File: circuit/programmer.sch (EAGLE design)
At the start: 23 parts, among them U1 TEENSY_3.0_DIL, X1 ESP01, X2 DIRTCHEAPRX-PROG-MINI, X3 DIRTCHEAPRX-PROG-NANO, X4 ESP01

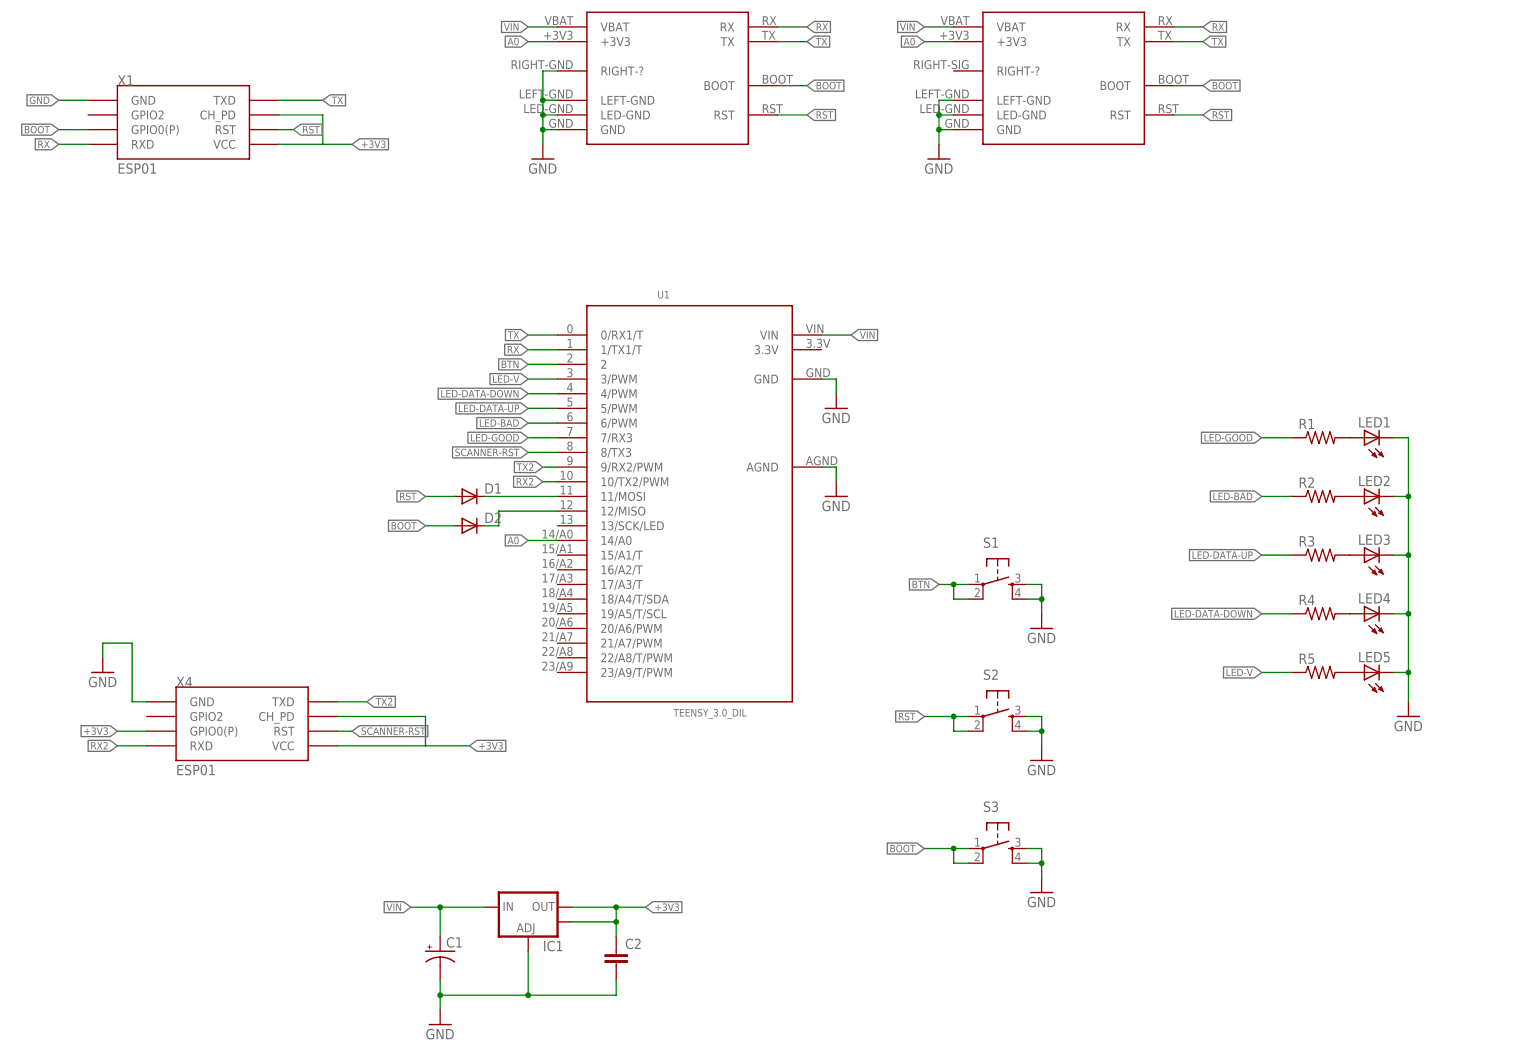
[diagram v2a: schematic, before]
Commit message: programmer, more vias, disconnectable boot signal
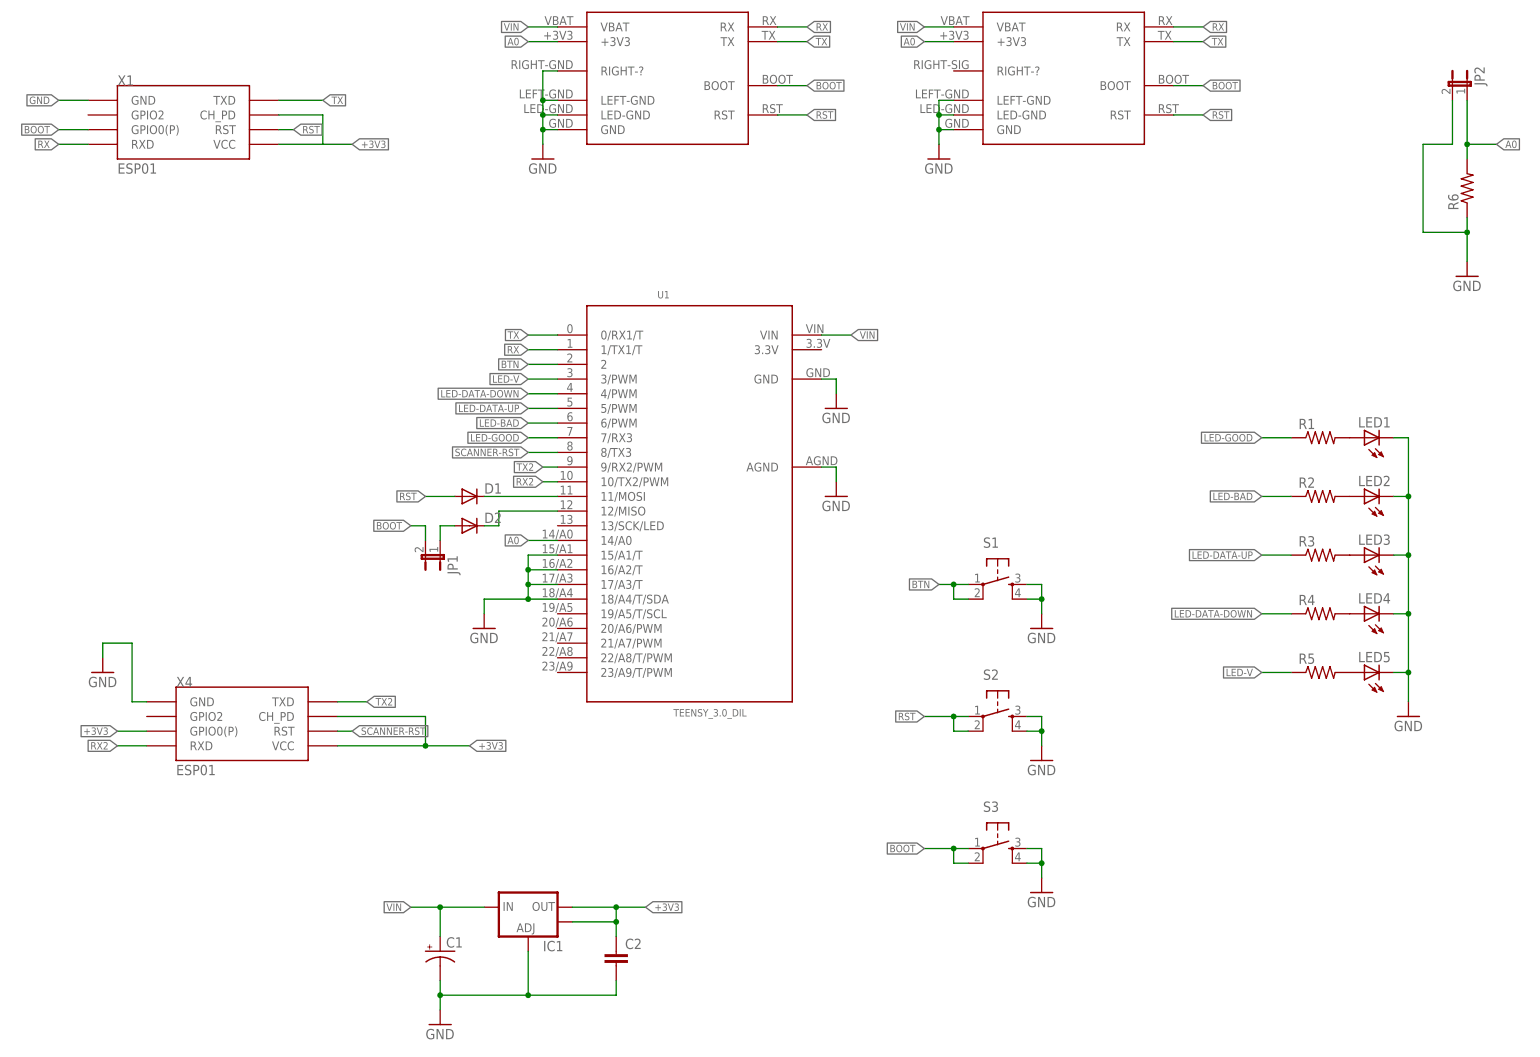
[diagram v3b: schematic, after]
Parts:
- added JP1, JP2: (no value), dirtcheaprx:JUMPER-2PTH_LOCK
- added R6: (no value), dirtcheaprx:RESISTOR0603-RES
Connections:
- new net N$8: D2.A, JP1.1
- net A0: now also JP2.1, R6.2
- net BOOT: now also JP1.2; no longer D2.A
- net GND: now also JP2.2, R6.1, U1.15/A1/T, U1.16/A2/T, U1.17/A3/T, U1.18/A4/T/SDA
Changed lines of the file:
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@@
 <part name="C1" library="dirtcheaprx" deviceset="CAP_POL" device="PTH1"/>
 <part name="C2" library="dirtcheaprx" deviceset="CAP" device="PTH2"/>
+<part name="JP1" library="dirtcheaprx" deviceset="JUMPER-2" device="PTH_LOCK"/>
+<part name="GND11" library="dirtcheaprx" deviceset="GND" device=""/>
+<part name="R6" library="dirtcheaprx" deviceset="RESISTOR" device="0603-RES"/>
+<part name="GND12" library="dirtcheaprx" deviceset="GND" device=""/>
+<part name="JP2" library="dirtcheaprx" deviceset="JUMPER-2" device="PTH_LOCK"/>
 </parts>
 <sheets>
@@
 <instance part="C1" gate="G$1" x="86.36" y="-66.04"/>
 <instance part="C2" gate="G$1" x="116.84" y="-68.58"/>
+<instance part="JP1" gate="A" x="86.36" y="2.54" rot="R180"/>
+<instance part="GND11" gate="1" x="93.98" y="-10.16"/>
+<instance part="R6" gate="G$1" x="264.16" y="66.04" rot="R90"/>
+<instance part="GND12" gate="1" x="264.16" y="50.8"/>
+<instance part="JP2" gate="A" x="264.16" y="83.82" rot="MR0"/>
 </instances>
 <busses>
@@
 <wire x1="83.82" y1="-25.4" x2="83.82" y2="-30.48" width="0.1524" layer="91"/>
 <label x="91.44" y="-30.48" size="1.27" layer="95" xref="yes"/>
+<junction x="83.82" y="-30.48"/>
 </segment>
 <segment>
@@
 </segment>
 <segment>
-<pinref part="D2" gate="G$1" pin="A"/>
-<wire x1="88.9" y1="7.62" x2="83.82" y2="7.62" width="0.1524" layer="91"/>
-<label x="83.82" y="7.62" size="1.27" layer="95" rot="R180" xref="yes"/>
-</segment>
-<segment>
 <pinref part="S3" gate="S" pin="1"/>
 <wire x1="177.8" y1="-48.26" x2="175.26" y2="-48.26" width="0.1524" layer="91"/>
@@
 <label x="170.18" y="-48.26" size="1.27" layer="95" rot="R180" xref="yes"/>
 <junction x="175.26" y="-48.26"/>
+</segment>
+<segment>
+<pinref part="JP1" gate="A" pin="2"/>
+<wire x1="83.82" y1="5.08" x2="83.82" y2="7.62" width="0.1524" layer="91"/>
+<wire x1="83.82" y1="7.62" x2="81.28" y2="7.62" width="0.1524" layer="91"/>
+<label x="81.28" y="7.62" size="1.27" layer="95" rot="R180" xref="yes"/>
 </segment>
 </net>
@@
 <junction x="86.36" y="-73.66"/>
 </segment>
+<segment>
+<pinref part="U1" gate="G$1" pin="15/A1/T"/>
+<wire x1="106.68" y1="2.54" x2="101.6" y2="2.54" width="0.1524" layer="91"/>
+<wire x1="101.6" y1="2.54" x2="101.6" y2="0" width="0.1524" layer="91"/>
+<pinref part="U1" gate="G$1" pin="18/A4/T/SDA"/>
+<wire x1="101.6" y1="0" x2="101.6" y2="-2.54" width="0.1524" layer="91"/>
+<wire x1="101.6" y1="-2.54" x2="101.6" y2="-5.08" width="0.1524" layer="91"/>
+<wire x1="101.6" y1="-5.08" x2="106.68" y2="-5.08" width="0.1524" layer="91"/>
+<pinref part="U1" gate="G$1" pin="17/A3/T"/>
+<wire x1="106.68" y1="-2.54" x2="101.6" y2="-2.54" width="0.1524" layer="91"/>
+<pinref part="U1" gate="G$1" pin="16/A2/T"/>
+<wire x1="106.68" y1="0" x2="101.6" y2="0" width="0.1524" layer="91"/>
+<pinref part="GND11" gate="1" pin="GND"/>
+<wire x1="101.6" y1="-5.08" x2="93.98" y2="-5.08" width="0.1524" layer="91"/>
+<wire x1="93.98" y1="-5.08" x2="93.98" y2="-7.62" width="0.1524" layer="91"/>
+<junction x="101.6" y="0"/>
+<junction x="101.6" y="-2.54"/>
+<junction x="101.6" y="-5.08"/>
+</segment>
+<segment>
+<pinref part="R6" gate="G$1" pin="1"/>
+<pinref part="GND12" gate="1" pin="GND"/>
+<wire x1="264.16" y1="53.34" x2="264.16" y2="58.42" width="0.1524" layer="91"/>
+<pinref part="JP2" gate="A" pin="2"/>
+<wire x1="264.16" y1="58.42" x2="264.16" y2="60.96" width="0.1524" layer="91"/>
+<wire x1="261.62" y1="81.28" x2="261.62" y2="73.66" width="0.1524" layer="91"/>
+<wire x1="261.62" y1="73.66" x2="256.54" y2="73.66" width="0.1524" layer="91"/>
+<wire x1="256.54" y1="73.66" x2="256.54" y2="58.42" width="0.1524" layer="91"/>
+<wire x1="256.54" y1="58.42" x2="264.16" y2="58.42" width="0.1524" layer="91"/>
+<junction x="264.16" y="58.42"/>
+</segment>
 </net>
 <net name="A0" class="0">
@@
 <wire x1="106.68" y1="5.08" x2="101.6" y2="5.08" width="0.1524" layer="91"/>
 <label x="101.6" y="5.08" size="1.27" layer="95" rot="R180" xref="yes"/>
+</segment>
+<segment>
+<pinref part="R6" gate="G$1" pin="2"/>
+<wire x1="264.16" y1="71.12" x2="264.16" y2="73.66" width="0.1524" layer="91"/>
+<wire x1="264.16" y1="73.66" x2="264.16" y2="81.28" width="0.1524" layer="91"/>
+<wire x1="264.16" y1="73.66" x2="269.24" y2="73.66" width="0.1524" layer="91"/>
+<label x="269.24" y="73.66" size="1.27" layer="95" xref="yes"/>
+<pinref part="JP2" gate="A" pin="1"/>
+<junction x="264.16" y="73.66"/>
 </segment>
 </net>
@@
 </segment>
 </net>
+<net name="N$8" class="0">
+<segment>
+<pinref part="D2" gate="G$1" pin="A"/>
+<pinref part="JP1" gate="A" pin="1"/>
+<wire x1="88.9" y1="7.62" x2="86.36" y2="7.62" width="0.1524" layer="91"/>
+<wire x1="86.36" y1="7.62" x2="86.36" y2="5.08" width="0.1524" layer="91"/>
+</segment>
+</net>

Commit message: gerber out, added some optional pull-up resistors
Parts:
- added R7, R8: (no value), dirtcheaprx:RESISTOR0603-RES
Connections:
- removed net +3V3: C2.1, IC1.OUT, IC1.OUT@1, X1.CH_PD, X1.VCC, X4.CH_PD, X4.GPIO0(P), X4.VCC
- new net 3.3V: C2.1, IC1.OUT, IC1.OUT@1, R7.2, R8.2, X1.CH_PD, X1.VCC, X4.CH_PD, X4.GPIO0(P), X4.VCC
- net BOOT: now also R7.1
- net RST: now also R8.1
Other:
- moved on the sheet: S2, S3
